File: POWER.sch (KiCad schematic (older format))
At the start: 24 parts, among them J6001 BATT1, J6002 BATT2_CELL2, J6003 BATT2_CELL1, J6004 BATT3_CELL2, J6005 BATT3_CELL1, U3 D24V50F5, U6001 D36V28F3, U6002 LM7809_TO220

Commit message: Reworked power system, added discrete regulators for hybrid servos
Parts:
- added J? (x2): BATT2_JST, Connector_JST:JST_XH_B4B-XH-A_1x04_P2.50mm_Vertical, symbol Connector_Generic:Conn_01x04
- added J?: BATT2_XT60, symbol XT60:XT60
- added R? (x6): 150k, symbol D24V50F5:R_US
- added R? (x2): 100k, symbol D24V50F5:R_US
- added R? (x2): 37.5k, symbol D24V50F5:R_US
- added R? (x2): 23k, symbol D24V50F5:R_US
- added U? (x2): D36V50F6, symbol D36V50F6:D36V50F6
- added U?: D24V50F5, D24V50F5:D24V50F5, symbol D24V50F5:D24V50F5
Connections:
- net labels added: 3V3_MCU_SUPPLY, 5V_AC_SERVO0, 5V_AC_SERVO1, 5V_MPU_SUPPLY, 6V_HYBRID_SERVO0, 6V_HYBRID_SERVO1, BATT2_CELL3, BATT3_CELL3, BATT4_CELL1, BATT4_CELL2, BATT5_CELL1, BATT5_CELL2
- net labels removed: +3V3, +5V
- wire segments 99 -> 192
- no-connect marks 2 -> 3
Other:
- note added: "4.5v -> 1.8v voltage dividers"
- note added: "AC SERVO POWER SYSTEM (BATT 3)"
- note added: "HYBRID SERVO POWER SYSTEM (BATT 2)"
- note added: "MPU + MCU POWER SYSTEM (BATT 1)"
- note added: "SL1 POWER SYSTEM (BATT 4)"
- note added: "SL2 POWER SYSTEM (BATT 5)"
- note removed: "NON-COMMERCIAL POWER SYSTEM (BATT 1)"
- note removed: "SL1 POWER SYSTEM (BATT 2)"
- note removed: "SL2 POWER SYSTEM (BATT 3)"
- moved on the sheet: C6001, C6002, J6001, J6002, J6003, R6001, R6002, R6003, R6004, R6005, R6006, R6007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

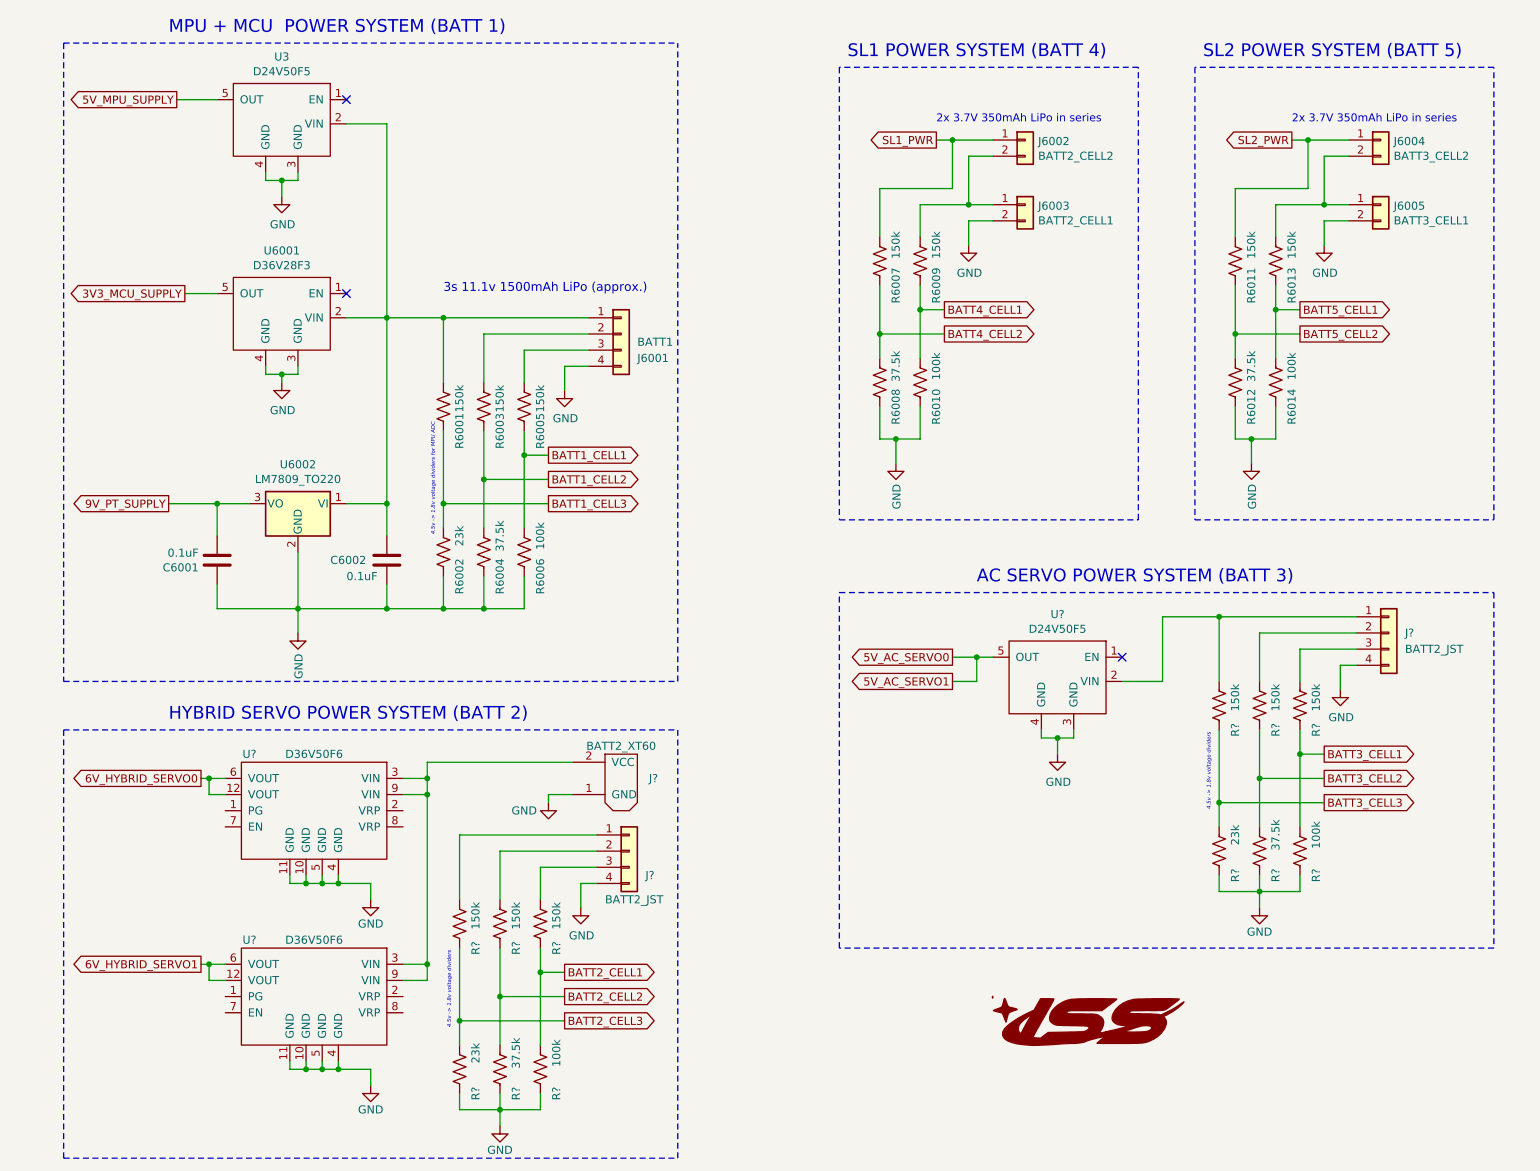
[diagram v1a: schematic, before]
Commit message: added minecraft with shaders (jetson nano) + switched to Teensy 4.1
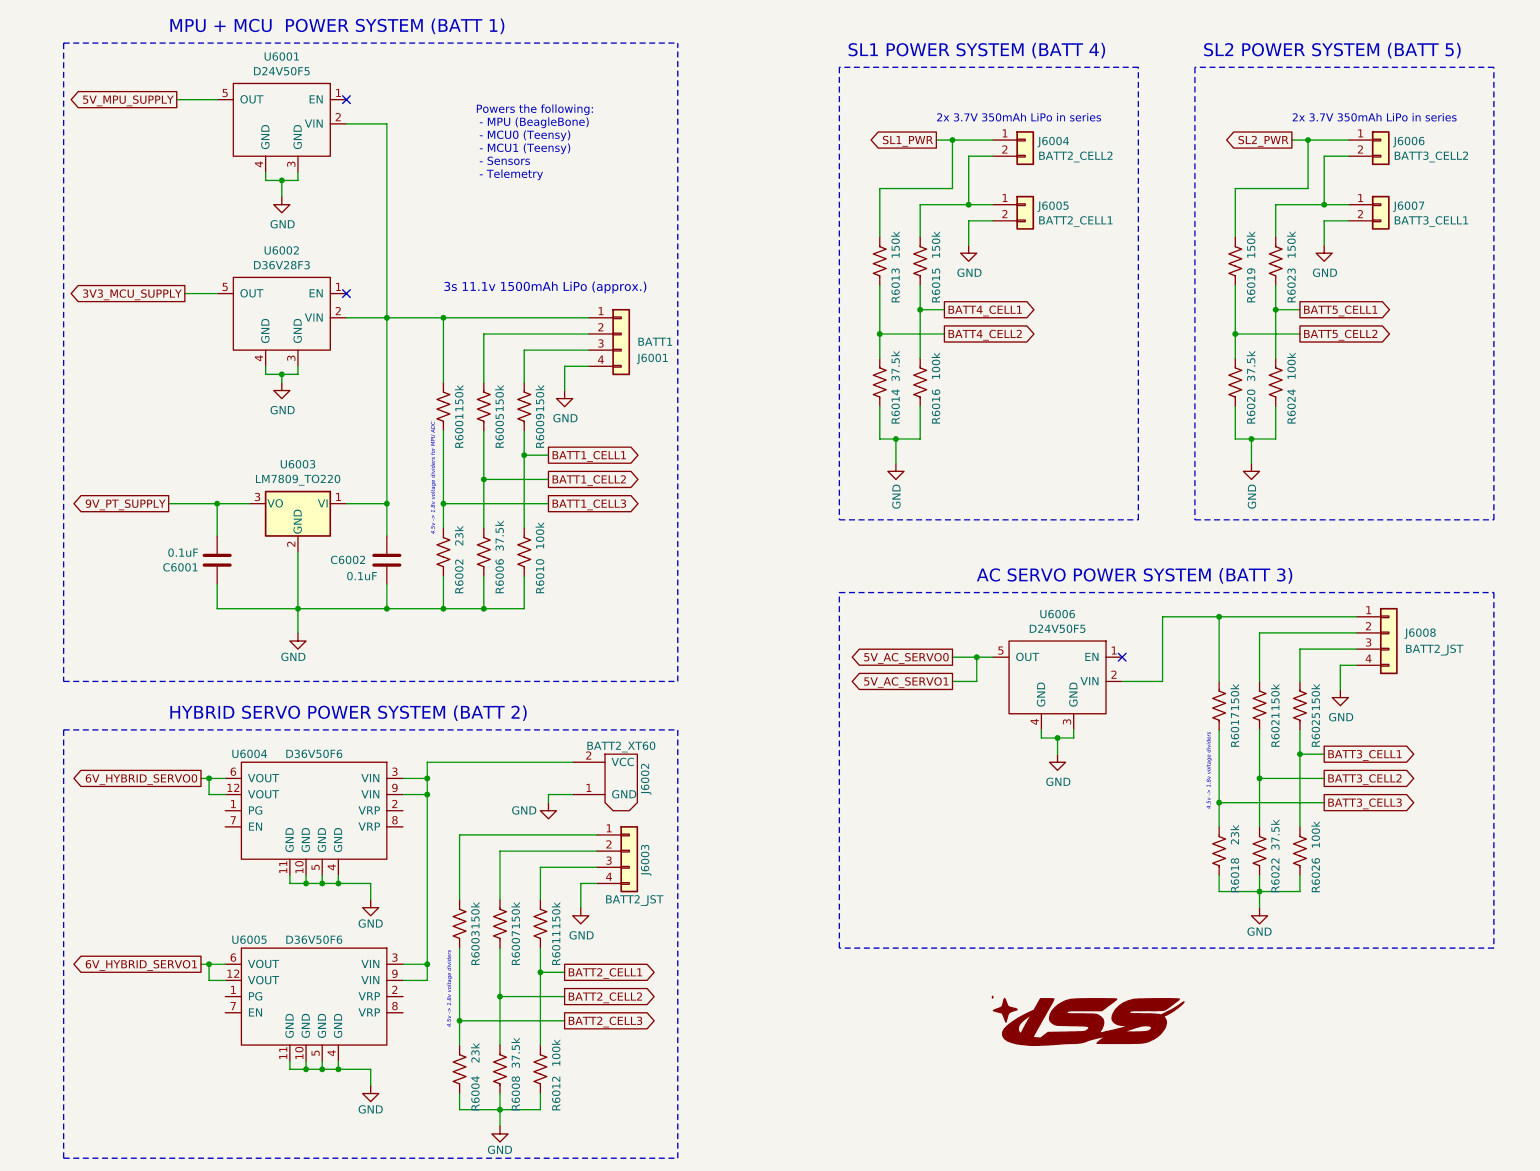
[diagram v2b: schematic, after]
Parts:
- J6002: renamed from J?; footprint (none) -> XT60:XT60
- gave numbers to parts that had none: 17
- renumbered J6002 to J6004, J6003 to J6005, J6004 to J6006, J6005 to J6007, R6003 to R6005, R6004 to R6006, R6005 to R6009, R6006 to R6010, R6007 to R6013, R6008 to R6014, R6009 to R6015, R6010 to R6016, R6011 to R6019, R6012 to R6020, R6013 to R6023, R6014 to R6024, U3 to U6001, U6001 to U6002, U6002 to U6003
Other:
- note added: "Powers the following:\n - MPU (BeagleBone)\n - MCU0 (Teensy)\n - MCU1 (Teensy)\n - Sensors\n - Telemetry"

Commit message: small fixes
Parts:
- J6004: value BATT2_CELL2 -> BATT4_CELL2
- J6005: value BATT2_CELL1 -> BATT4_CELL1
- J6006: value BATT3_CELL2 -> BATT5_CELL2
- J6007: value BATT3_CELL1 -> BATT5_CELL1
- J6008: value BATT2_JST -> BATT3_JST
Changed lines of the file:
@@
 P 7200 1750
 F 0 "J6005" H 7280 1742 50  0000 L CNN
-F 1 "BATT2_CELL1" H 7280 1651 50  0000 L CNN
+F 1 "BATT4_CELL1" H 7280 1651 50  0000 L CNN
 F 2 "Connector_JST:JST_PH_B2B-PH-K_1x02_P2.00mm_Vertical" H 7200 1750 50  0001 C CNN
 F 3 "~" H 7200 1750 50  0001 C CNN
@@
 P 7200 1350
 F 0 "J6004" H 7280 1342 50  0000 L CNN
-F 1 "BATT2_CELL2" H 7280 1251 50  0000 L CNN
+F 1 "BATT4_CELL2" H 7280 1251 50  0000 L CNN
 F 2 "Connector_JST:JST_PH_B2B-PH-K_1x02_P2.00mm_Vertical" H 7200 1350 50  0001 C CNN
 F 3 "~" H 7200 1350 50  0001 C CNN
@@
 P 9400 1750
 F 0 "J6007" H 9480 1742 50  0000 L CNN
-F 1 "BATT3_CELL1" H 9480 1651 50  0000 L CNN
+F 1 "BATT5_CELL1" H 9480 1651 50  0000 L CNN
 F 2 "Connector_JST:JST_PH_B2B-PH-K_1x02_P2.00mm_Vertical" H 9400 1750 50  0001 C CNN
 F 3 "~" H 9400 1750 50  0001 C CNN
@@
 P 9400 1350
 F 0 "J6006" H 9480 1342 50  0000 L CNN
-F 1 "BATT3_CELL2" H 9480 1251 50  0000 L CNN
+F 1 "BATT5_CELL2" H 9480 1251 50  0000 L CNN
 F 2 "Connector_JST:JST_PH_B2B-PH-K_1x02_P2.00mm_Vertical" H 9400 1350 50  0001 C CNN
 F 3 "~" H 9400 1350 50  0001 C CNN
@@
 P 9450 4400
 F 0 "J6008" H 9550 4400 50  0000 L CNN
-F 1 "BATT2_JST" H 9550 4300 50  0000 L CNN
+F 1 "BATT3_JST" H 9550 4300 50  0000 L CNN
 F 2 "Connector_JST:JST_XH_B4B-XH-A_1x04_P2.50mm_Vertical" H 9450 4400 50  0001 C CNN
 F 3 "~" H 9450 4400 50  0001 C CNN

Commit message: started pcb layout
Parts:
- U6004, U6005: footprint (none) -> D36V50F6:D36V50F6
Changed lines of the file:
@@
 F 0 "U6004" H 3200 5150 50  0000 C CNN
 F 1 "D36V50F6" H 2800 5150 50  0000 C CNN
-F 2 "" H 2800 5150 50  0001 C CNN
+F 2 "D36V50F6:D36V50F6" H 2800 5150 50  0001 C CNN
 F 3 "" H 2800 5150 50  0001 C CNN
 	1    2800 5150
@@
 F 0 "U6005" H 3200 6300 50  0000 C CNN
 F 1 "D36V50F6" H 2800 6300 50  0000 C CNN
-F 2 "" H 2800 6300 50  0001 C CNN
+F 2 "D36V50F6:D36V50F6" H 2800 6300 50  0001 C CNN
 F 3 "" H 2800 6300 50  0001 C CNN
 	1    2800 6300
